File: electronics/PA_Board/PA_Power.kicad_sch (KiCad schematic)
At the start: 37 parts, among them J5 Conn_01x02, Q1 SUD09P10-195, U4 MP1584, U5 MCP4725xxx-xCH, U6 AP2204K-ADJ, U7 TLV70233, U8 INA219AxD

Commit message: PCB updates and gerbers
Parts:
- L2: footprint Inductor_SMD:L_7.3x7.3_H3.5 -> Inductor_SMD:L_7.3x7.3_H4.5
- U4: footprint Package_SO:SOIC-8-1EP_3.9x4.9mm_P1.27mm_EP2.41x3.3mm_ThermalVias -> Package_SO:SOIC-8-1EP_3.9x4.9mm_P1.27mm_EP2.41x3.3mm
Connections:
- net VDD_GAIN renamed +5V
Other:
- moved on the sheet: C26, U8

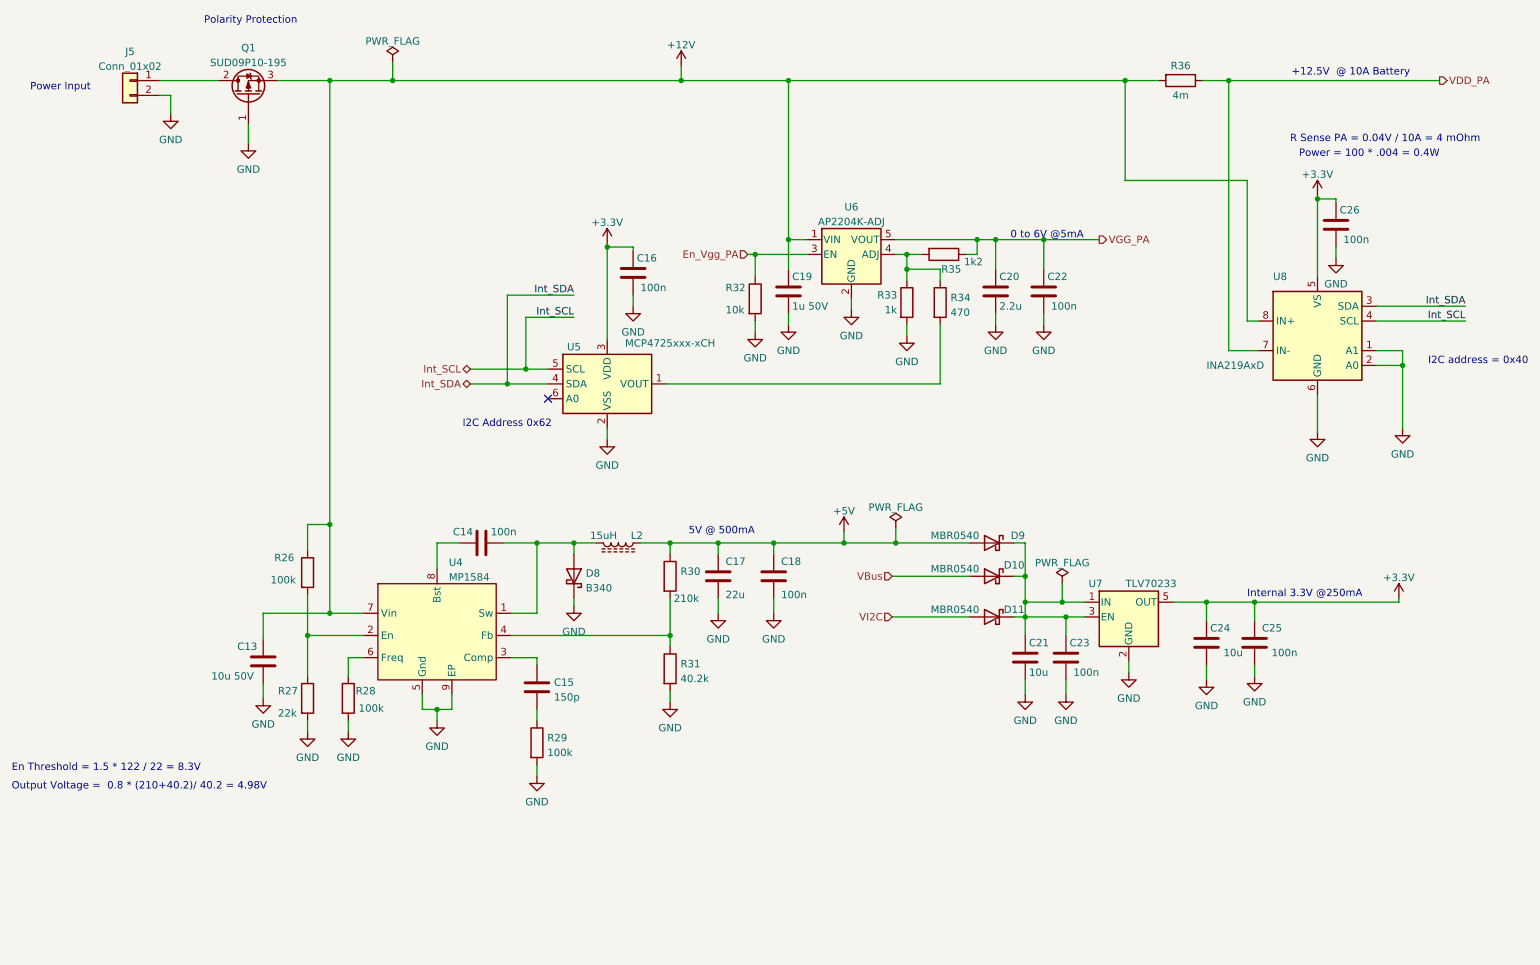
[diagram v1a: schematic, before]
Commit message: Update Kicad Schematic and PCB
Fixed: D8 was reversed, Q2 wrong footprint.
Some component values added or changed
Documentation added
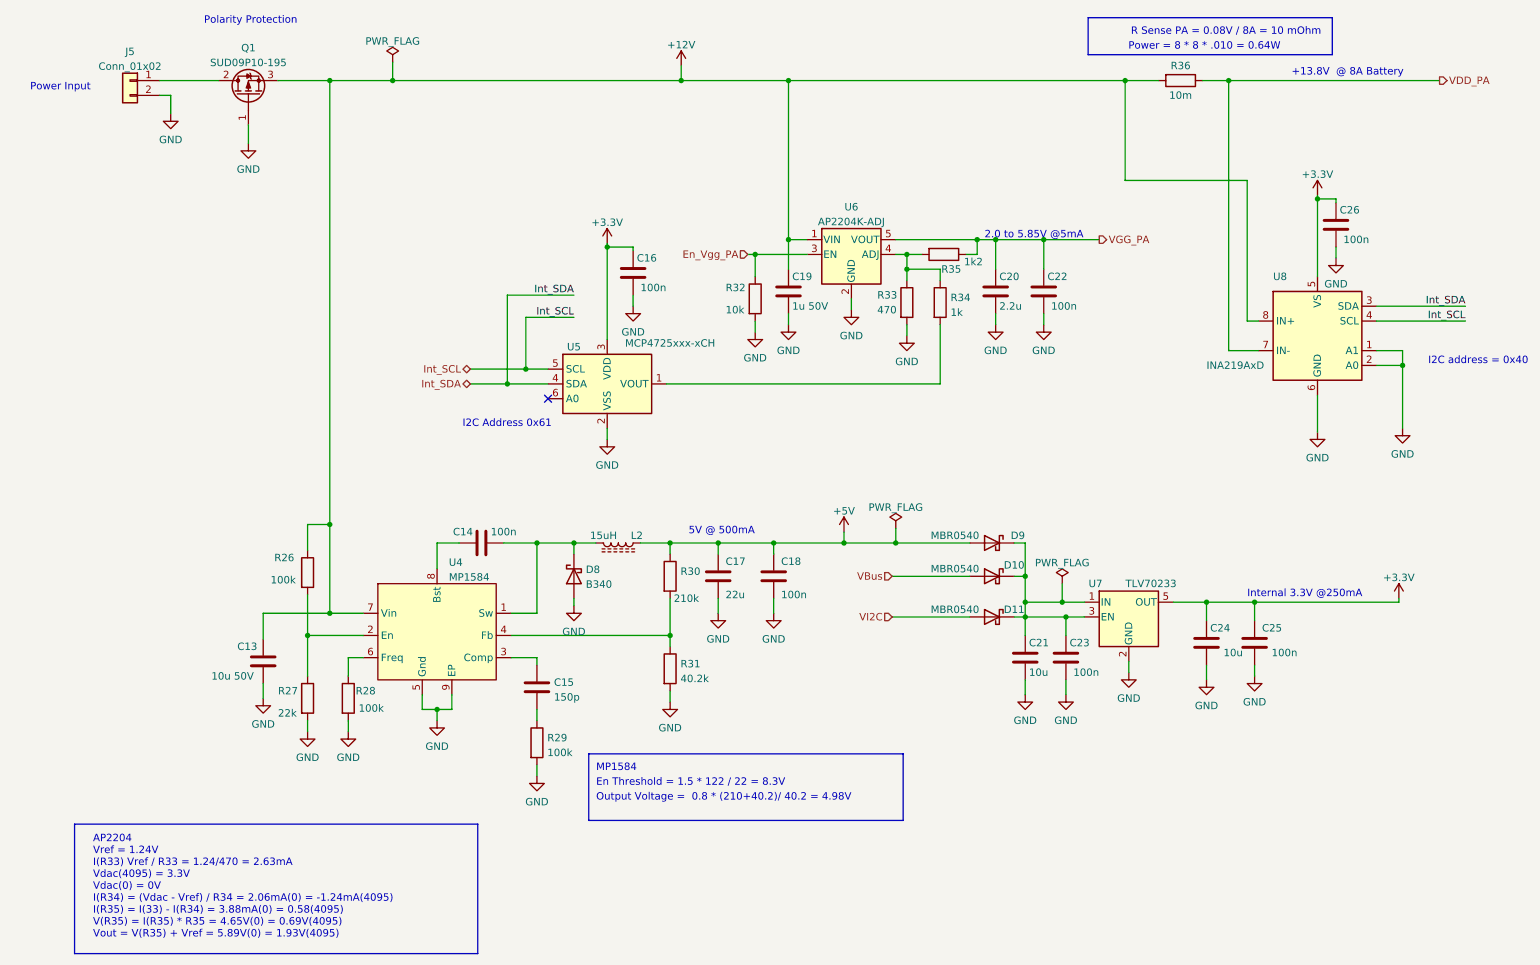
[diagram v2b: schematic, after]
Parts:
- R33: value 1k -> 470
- R34: value 470 -> 1k
- R36: value 4m -> 10m
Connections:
- net GND: now also D8.2 (A); no longer D8.1 (K)
- net at C14.1, L2.2, U4.1 (Sw): now also D8.1 (K); no longer D8.2 (A)
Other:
- note added: "+13.8V @ 8A Battery"
- note added: "2.0 to 5.85V @5mA"
- note added: "AP2204 Vref = 1.24V I(R33) Vref / R33 = 1.24/470 = 2.63mA Vdac(4095) = 3.3V Vdac(0) = 0V I(R34) = (Vdac - Vref) / R34 = 2.06mA(0) = -1.24mA(4095) I(R35) = I(33) - I(R34) = 3.88mA(0) = 0.58(4095) V(R35) = I(R35) * R35 = 4.65V(0) = 0.69V(4095) Vout = V(R35) + Vref = 5.89V(0) = 1.93V(4095)"
- note added: "I2C Address 0x61"
- note added: "MP1584"
- note added: "Power = 8 * 8 * .010 = 0.64W"
- note added: "R Sense PA = 0.08V / 8A = 10 mOhm"
- note removed: "+12.5V @ 10A Battery"
- note removed: "0 to 6V @5mA"
- note removed: "I2C Address 0x62"
- note removed: "Power = 100 * .004 = 0.4W"
- note removed: "R Sense PA = 0.04V / 10A = 4 mOhm"
- moved on the sheet: D8
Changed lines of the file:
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@@
+    (stroke (width 0) (type default) (color 0 0 0 0))
+  )
+  (polyline (pts (xy 116.205 147.955) (xy 170.18 147.955))
     (stroke (width 0) (type default) (color 0 0 0 0))
   )
@@
     (stroke (width 0) (type default) (color 0 0 0 0))
   )
+  (polyline (pts (xy 27.94 160.02) (xy 27.94 182.245))
+    (stroke (width 0) (type default) (color 0 0 0 0))
+  )
   (wire (pts (xy 119.38 60.325) (xy 119.38 60.96))
     (stroke (width 0) (type default) (color 0 0 0 0))
@@
     (stroke (width 0) (type default) (color 0 0 0 0))
   )
+  (polyline (pts (xy 201.93 21.59) (xy 201.93 27.94))
+    (stroke (width 0) (type default) (color 0 0 0 0))
+  )
   (wire (pts (xy 251.46 78.74) (xy 255.905 78.74))
     (stroke (width 0) (type default) (color 0 0 0 0))
@@
     (stroke (width 0) (type default) (color 0 0 0 0))
   )
+  (polyline (pts (xy 27.94 182.245) (xy 97.155 182.245))
+    (stroke (width 0) (type default) (color 0 0 0 0))
+  )
   (wire (pts (xy 189.23 117.475) (xy 191.135 117.475))
     (stroke (width 0) (type default) (color 0 0 0 0))
@@
     (stroke (width 0) (type default) (color 0 0 0 0))
   )
+  (polyline (pts (xy 27.94 160.02) (xy 97.155 160.02))
+    (stroke (width 0) (type default) (color 0 0 0 0))
+  )
   (wire (pts (xy 132.08 29.845) (xy 132.08 32.385))
     (stroke (width 0) (type default) (color 0 0 0 0))
   )
+  (polyline (pts (xy 116.205 147.955) (xy 116.205 159.385))
+    (stroke (width 0) (type default) (color 0 0 0 0))
+  )
   (wire (pts (xy 241.3 52.705) (xy 241.3 52.07))
     (stroke (width 0) (type default) (color 0 0 0 0))
@@
     (stroke (width 0) (type default) (color 0 0 0 0))
   )
+  (polyline (pts (xy 97.155 182.245) (xy 97.155 160.02))
+    (stroke (width 0) (type default) (color 0 0 0 0))
+  )
   (wire (pts (xy 255.27 121.285) (xy 255.27 121.92))
     (stroke (width 0) (type default) (color 0 0 0 0))
@@
     (stroke (width 0) (type default) (color 0 0 0 0))
   )
+  (polyline (pts (xy 201.93 27.94) (xy 243.84 27.94))
+    (stroke (width 0) (type default) (color 0 0 0 0))
+  )
   (wire (pts (xy 107.315 131.445) (xy 102.87 131.445))
     (stroke (width 0) (type default) (color 0 0 0 0))
@@
     (stroke (width 0) (type default) (color 0 0 0 0))
   )
+  (polyline (pts (xy 116.205 159.385) (xy 170.18 159.385))
+    (stroke (width 0) (type default) (color 0 0 0 0))
+  )
   (wire (pts (xy 90.17 111.76) (xy 90.17 116.205))
     (stroke (width 0) (type default) (color 0 0 0 0))
@@
     (stroke (width 0) (type default) (color 0 0 0 0))
   )
+  (polyline (pts (xy 243.84 27.94) (xy 243.84 21.59))
+    (stroke (width 0) (type default) (color 0 0 0 0))
+  )
   (wire (pts (xy 107.315 111.76) (xy 113.665 111.76))
     (stroke (width 0) (type default) (color 0 0 0 0))
@@
     (stroke (width 0) (type default) (color 0 0 0 0))
   )
+  (polyline (pts (xy 201.93 21.59) (xy 243.84 21.59))
+    (stroke (width 0) (type default) (color 0 0 0 0))
+  )
   (wire (pts (xy 208.28 32.385) (xy 213.995 32.385))
     (stroke (width 0) (type default) (color 0 0 0 0))
@@
   )
   (wire (pts (xy 230.505 132.715) (xy 230.505 134.62))
+    (stroke (width 0) (type default) (color 0 0 0 0))
+  )
+  (polyline (pts (xy 170.18 159.385) (xy 170.18 147.955))
     (stroke (width 0) (type default) (color 0 0 0 0))
   )
@@
     (effects (font (size 1.27 1.27)) (justify left bottom))
   )
-  (text "0 to 6V @5mA" (at 188.595 59.69 0)
+  (text "2.0 to 5.85V @5mA" (at 184.15 59.69 0)
     (effects (font (size 1.27 1.27)) (justify left bottom))
   )
-  (text "I2C Address 0x62" (at 109.855 92.075 180)
+  (text "I2C Address 0x61" (at 109.855 92.075 180)
     (effects (font (size 1.27 1.27)) (justify right bottom))
   )
-  (text "+12.5V  @ 10A Battery" (at 236.855 31.75 0)
+  (text "+13.8V  @ 8A Battery" (at 236.855 31.75 0)
     (effects (font (size 1.27 1.27)) (justify left bottom))
   )
@@
     (effects (font (size 1.27 1.27)) (justify right bottom))
   )
+  (text "MP1584" (at 117.475 151.13 0)
+    (effects (font (size 1.27 1.27)) (justify left bottom))
+  )
   (text "Internal 3.3V @250mA" (at 229.235 121.285 0)
     (effects (font (size 1.27 1.27)) (justify left bottom))
   )
-  (text "R Sense PA = 0.04V / 10A = 4 mOhm" (at 269.24 43.18 180)
+  (text "AP2204\nVref = 1.24V\nI(R33) Vref / R33 = 1.24/470 = 2.63mA\nVdac(4095) = 3.3V\nVdac(0) = 0V\nI(R34) = (Vdac - Vref) / R34 = 2.06mA(0) = -1.24mA(4095)\nI(R35) = I(33) - I(R34) = 3.88mA(0) = 0.58(4095)\nV(R35) = I(R35) * R35 = 4.65V(0) = 0.69V(4095)\nVout = V(R35) + Vref = 5.89V(0) = 1.93V(4095)\n"
+    (at 31.115 179.705 0)
+    (effects (font (size 1.27 1.27)) (justify left bottom))
+  )
+  (text "R Sense PA = 0.08V / 8A = 10 mOhm" (at 241.935 24.765 180)
     (effects (font (size 1.27 1.27)) (justify right bottom))
   )
@@
     (effects (font (size 1.27 1.27)) (justify left bottom))
   )
-  (text "Power = 100 * .004 = 0.4W" (at 262.255 45.72 180)
+  (text "Power = 8 * 8 * .010 = 0.64W" (at 234.95 27.305 180)
     (effects (font (size 1.27 1.27)) (justify right bottom))
   )
-  (text "Output Voltage =  0.8 * (210+40.2)/ 40.2 = 4.98V" (at 17.145 154.305 0)
+  (text "Output Voltage =  0.8 * (210+40.2)/ 40.2 = 4.98V" (at 117.475 156.21 0)
     (effects (font (size 1.27 1.27)) (justify left bottom))
   )
-  (text "En Threshold = 1.5 * 122 / 22 = 8.3V" (at 17.145 151.13 0)
+  (text "En Threshold = 1.5 * 122 / 22 = 8.3V" (at 117.475 153.67 0)
     (effects (font (size 1.27 1.27)) (justify left bottom))
   )
@@
   )
   (symbol (lib_id "power:GND") (at 67.945 144.145 0) (unit 1)
-    (in_bom yes) (on_board yes) (fields_autoplaced)
+    (in_bom yes) (on_board yes)
     (property "Reference" "#PWR042" (id 0) (at 67.945 150.495 0)
       (effects (font (size 1.27 1.27)) hide)
@@
       (effects (font (size 1.27 1.27)) (justify left))
     )
-    (property "Value" "1k" (id 1) (at 167.005 71.755 0)
+    (property "Value" "470" (id 1) (at 165.735 71.755 0)
       (effects (font (size 1.27 1.27)) (justify left))
     )
@@
     (in_bom yes) (on_board yes)
     (property "Reference" "R36" (id 0) (at 217.805 29.845 90))
-    (property "Value" "4m" (id 1) (at 217.805 34.925 90))
+    (property "Value" "10m" (id 1) (at 217.805 34.925 90))
     (property "Footprint" "Resistor_SMD:R_0612_1632Metric" (id 2) (at 217.805 30.607 90)
       (effects (font (size 1.27 1.27)) hide)
@@
     (pin "1")
   )
-  (symbol (lib_id "Device:D_Schottky") (at 113.665 117.475 270) (mirror x) (unit 1)
-    (in_bom yes) (on_board yes) (fields_autoplaced)
-    (property "Reference" "D8" (id 0) (at 115.697 116.9578 90)
-      (effects (font (size 1.27 1.27)) (justify left))
-    )
-    (property "Value" "B340" (id 1) (at 115.697 119.4947 90)
-      (effects (font (size 1.27 1.27)) (justify left))
+  (symbol (lib_id "Device:D_Schottky") (at 113.665 117.475 90) (mirror x) (unit 1)
+    (in_bom yes) (on_board yes) (fields_autoplaced)
+    (property "Reference" "D8" (id 0) (at 115.697 116.3228 90)
+      (effects (font (size 1.27 1.27)) (justify right))
+    )
+    (property "Value" "B340" (id 1) (at 115.697 118.8597 90)
+      (effects (font (size 1.27 1.27)) (justify right))
     )
     (property "Footprint" "Diode_SMD:D_SMA" (id 2) (at 113.665 117.475 0)
@@
   )
   (symbol (lib_id "power:GND") (at 74.93 144.145 0) (unit 1)
-    (in_bom yes) (on_board yes) (fields_autoplaced)
+    (in_bom yes) (on_board yes)
     (property "Reference" "#PWR043" (id 0) (at 74.93 150.495 0)
       (effects (font (size 1.27 1.27)) hide)
@@
       (effects (font (size 1.27 1.27)) (justify left))
     )
-    (property "Value" "470" (id 1) (at 178.308 72.1872 0)
-      (effects (font (size 1.27 1.27)) (justify left))
-    )
+    (property "Value" "1k" (id 1) (at 178.308 72.1872 0)
+      (effects (font (size 1.27 1.27)) (justify left))
+    )

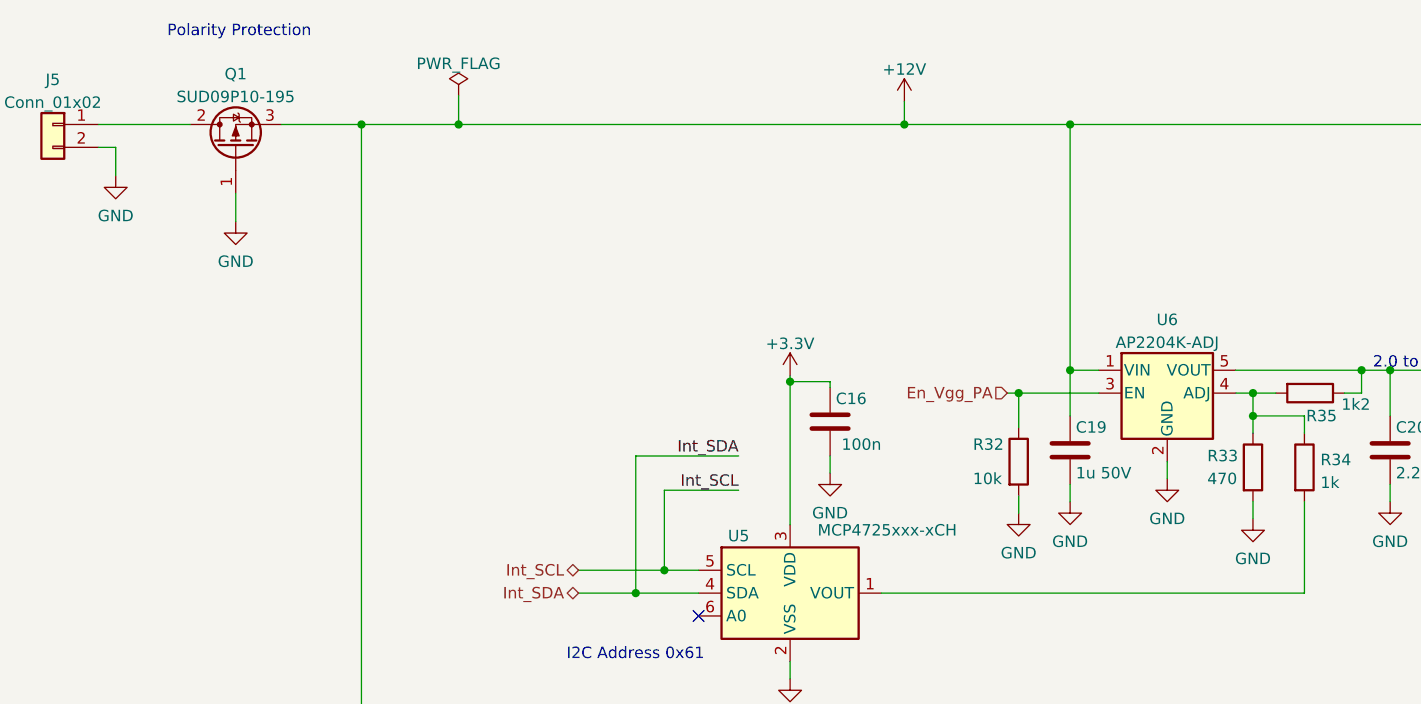
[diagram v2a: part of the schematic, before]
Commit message: Add PA Board tests
Add PA Board Arduino Tests
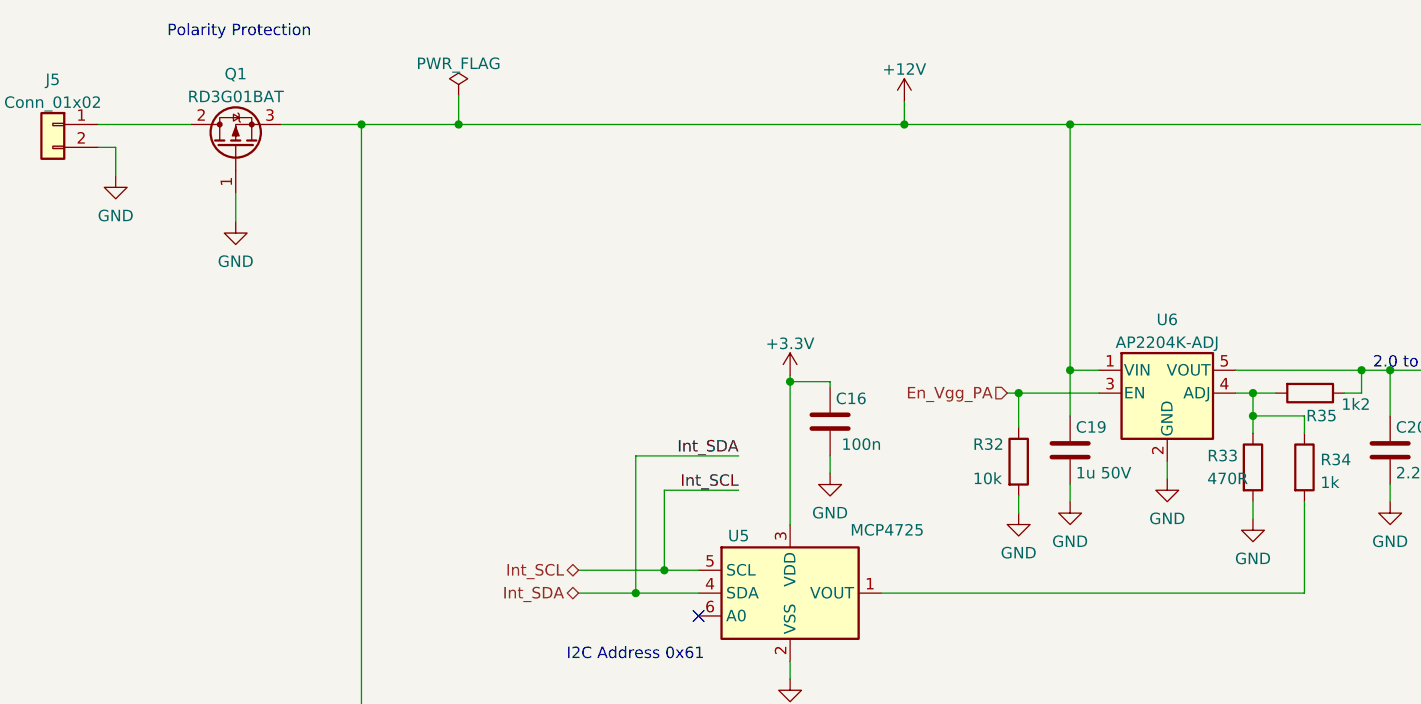
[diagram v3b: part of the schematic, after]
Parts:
- Q1: value SUD09P10-195 -> RD3G01BAT
- R33: value 470 -> 470R
- U5: value MCP4725xxx-xCH -> MCP4725
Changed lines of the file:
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@@
     (in_bom yes) (on_board yes)
     (property "Reference" "U5" (id 0) (at 113.665 78.105 0))
-    (property "Value" "MCP4725xxx-xCH" (id 1) (at 130.175 77.47 0))
+    (property "Value" "MCP4725" (id 1) (at 130.175 77.47 0))
     (property "Footprint" "Package_TO_SOT_SMD:SOT-23-6" (id 2) (at 119.38 90.805 0)
       (effects (font (size 1.27 1.27)) hide)
@@
       (effects (font (size 1.27 1.27)) (justify left))
     )
-    (property "Value" "470" (id 1) (at 165.735 71.755 0)
+    (property "Value" "470R" (id 1) (at 165.735 71.755 0)
       (effects (font (size 1.27 1.27)) (justify left))
     )
@@
     (in_bom yes) (on_board yes) (fields_autoplaced)
     (property "Reference" "Q1" (id 0) (at 57.785 26.7802 90))
-    (property "Value" "SUD09P10-195" (id 1) (at 57.785 29.3171 90))
+    (property "Value" "RD3G01BAT" (id 1) (at 57.785 29.3171 90))
     (property "Footprint" "Package_TO_SOT_SMD:TO-252-2" (id 2) (at 59.69 29.972 0)
       (effects (font (size 1.27 1.27) italic) (justify left) hide)
     )
-    (property "Datasheet" "https://www.vishay.com/docs/65903/SUD09P10.pdf" (id 3) (at 57.785 34.925 0)
-      (effects (font (size 1.27 1.27)) hide)
-    )
+    (property "Datasheet" "" (id 3) (at 57.785 34.925 0)
+      (effects (font (size 1.27 1.27)) hide)
+    )
